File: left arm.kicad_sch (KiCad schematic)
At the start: 11 parts, among them M21 Stepper_Motor_bipolar, M22 Motor_DC, M23 RHP020N06, M24 Motor_Servo, M25 Motor_Servo, M26 Motor_Servo, M27 Stepper_Motor_bipolar, M28 Stepper_Motor_bipolar

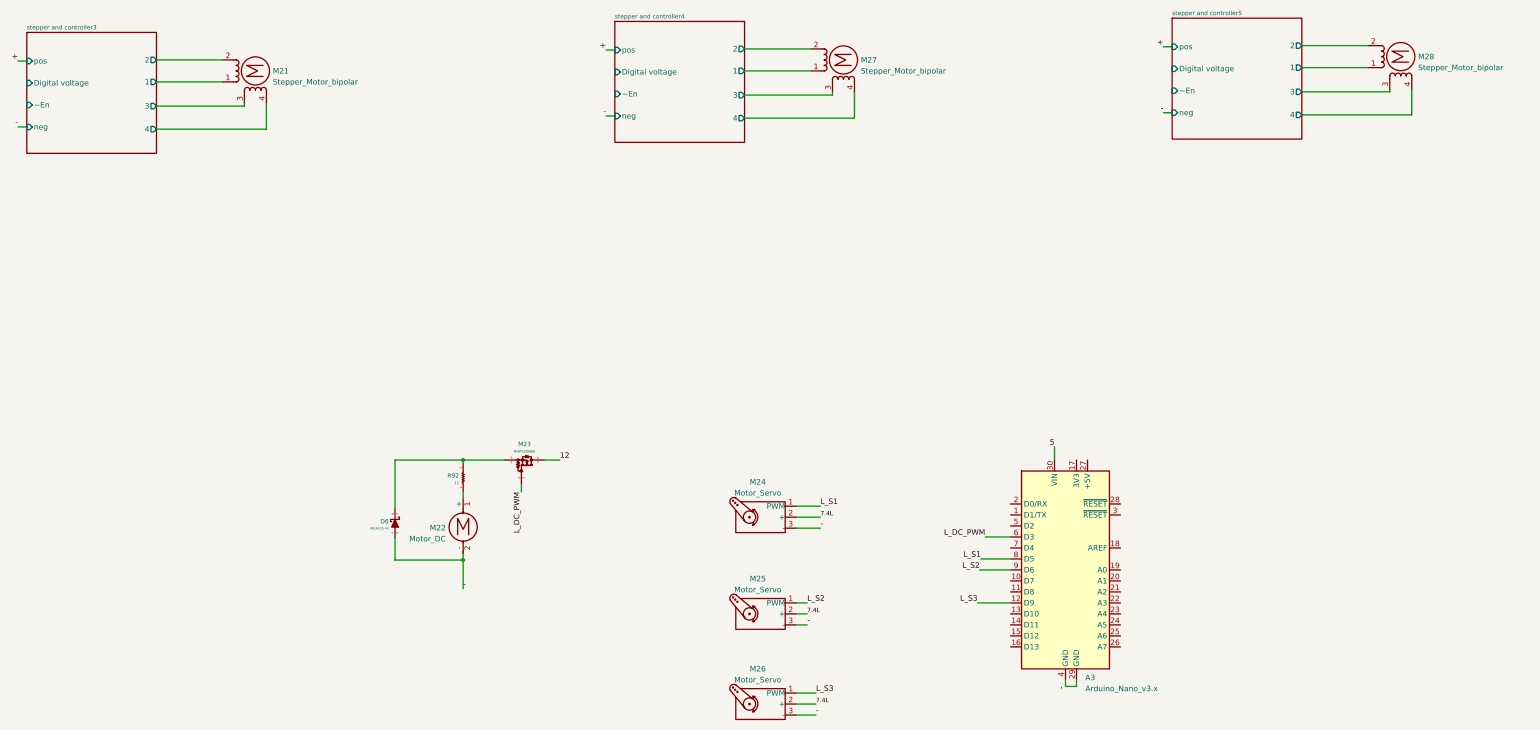
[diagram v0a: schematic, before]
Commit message: base schematic and PCB made
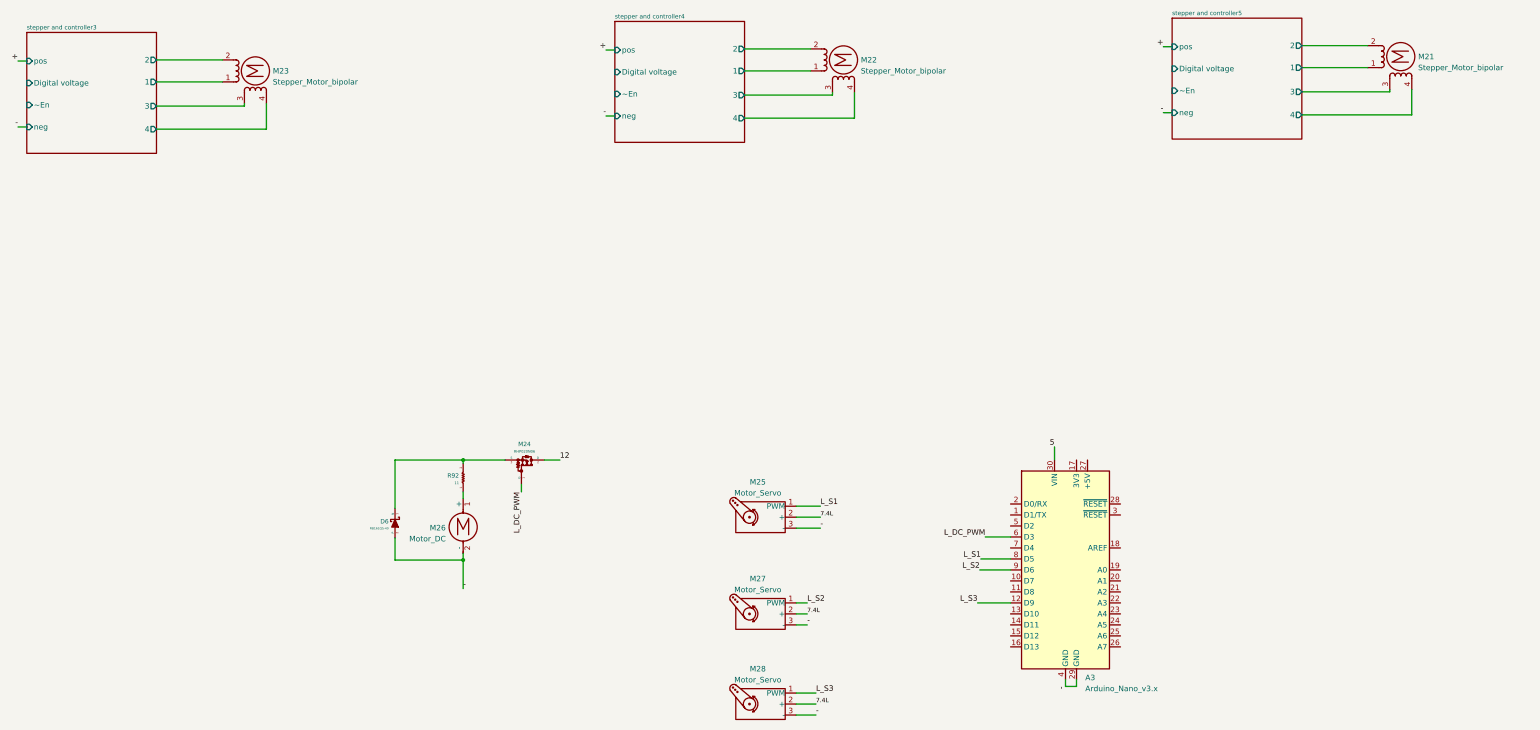
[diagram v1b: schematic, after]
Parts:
- D6: footprint my_footprints:RB161QS-40T18R -> Diodes:RB161QS-40T18R; symbol diodes:RB161QS-40 -> Diodes:RB161QS-40
- M21: renamed from M28; footprint (none) -> Connectors:1-350944-0
- M22: renamed from M27; footprint (none) -> Connectors:1-350944-0
- M23: renamed from M21; footprint (none) -> Connectors:1-350944-0
- M24: renamed from M23; footprint my_footprints:RHP020N06T100 -> E-MOSFETs:RHP020N06T100
- R92: footprint my_footprints:MCR03EZPFX -> Resistors:MCR03EZPFX; symbol resistors:MCR03EZPFX -> Resistors:MCR03EZPFX
- renumbered M24 to M25, M22 to M26, M25 to M27, M26 to M28
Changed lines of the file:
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@@
     (effects (font (size 1 1)) (justify left bottom))
   )
-  (symbol (lib_id "resistors:MCR03EZPFX") (at 131.572 140.208 270) (mirror x) (unit 1)
+  (symbol (lib_id "Resistors:MCR03EZPFX") (at 131.572 140.208 270) (mirror x) (unit 1)
     (in_bom yes) (on_board yes) (fields_autoplaced)
     (property "Reference" "R92" (id 0) (at 130.6068 139.7467 90)
@@
       (effects (font (size 0.6 0.6)) (justify right))
     )
-    (property "Footprint" "my_footprints:MCR03EZPFX" (id 2) (at 123.698 140.208 0)
+    (property "Footprint" "Resistors:MCR03EZPFX" (id 2) (at 123.698 140.208 0)
       (effects (font (size 1.27 1.27)) hide)
     )
@@
     (pin "2")
   )
-  (symbol (lib_id "diodes:RB161QS-40") (at 115.824 150.876 90) (mirror x) (unit 1)
+  (symbol (lib_id "Diodes:RB161QS-40") (at 115.824 150.876 90) (mirror x) (unit 1)
     (in_bom yes) (on_board yes) (fields_autoplaced)
     (property "Reference" "D6" (id 0) (at 114.3508 150.3333 90)
@@
       (effects (font (size 0.5 0.5)) (justify left))
     )
-    (property "Footprint" "my_footprints:RB161QS-40T18R" (id 2) (at 126.492 150.876 0)
+    (property "Footprint" "Diodes:RB161QS-40T18R" (id 2) (at 126.492 150.876 0)
       (effects (font (size 1.524 1.524)) hide)
     )
@@
   (symbol (lib_id "Motor:Motor_Servo") (at 200.914 149.352 0) (mirror y) (unit 1)
     (in_bom yes) (on_board yes) (fields_autoplaced)
-    (property "Reference" "M24" (id 0) (at 199.6551 141.2294 0))
+    (property "Reference" "M25" (id 0) (at 199.6551 141.2294 0))
     (property "Value" "Motor_Servo" (id 1) (at 199.6551 143.7663 0))
     (property "Footprint" "" (id 2) (at 200.914 154.178 0)
@@
   (symbol (lib_id "Motor:Motor_Servo") (at 200.914 192.532 0) (mirror y) (unit 1)
     (in_bom yes) (on_board yes) (fields_autoplaced)
-    (property "Reference" "M26" (id 0) (at 199.6551 184.4094 0))
+    (property "Reference" "M28" (id 0) (at 199.6551 184.4094 0))
     (property "Value" "Motor_Servo" (id 1) (at 199.6551 186.9463 0))
     (property "Footprint" "" (id 2) (at 200.914 197.358 0)
@@
   (symbol (lib_id "Motor:Stepper_Motor_bipolar") (at 348.234 42.926 90) (unit 1)
     (in_bom yes) (on_board yes) (fields_autoplaced)
-    (property "Reference" "M28" (id 0) (at 352.2472 42.9422 90)
+    (property "Reference" "M21" (id 0) (at 352.2472 42.9422 90)
       (effects (font (size 1.27 1.27)) (justify right))
     )
@@
       (effects (font (size 1.27 1.27)) (justify right))
     )
-    (property "Footprint" "" (id 2) (at 348.488 42.672 0)
+    (property "Footprint" "Connectors:1-350944-0" (id 2) (at 348.488 42.672 0)
       (effects (font (size 1.27 1.27)) hide)
     )
@@
   (symbol (lib_id "Motor:Stepper_Motor_bipolar") (at 83.566 46.228 90) (unit 1)
     (in_bom yes) (on_board yes) (fields_autoplaced)
-    (property "Reference" "M21" (id 0) (at 87.5792 46.2442 90)
+    (property "Reference" "M23" (id 0) (at 87.5792 46.2442 90)
       (effects (font (size 1.27 1.27)) (justify right))
     )
@@
       (effects (font (size 1.27 1.27)) (justify right))
     )
-    (property "Footprint" "" (id 2) (at 83.82 45.974 0)
+    (property "Footprint" "Connectors:1-350944-0" (id 2) (at 83.82 45.974 0)
       (effects (font (size 1.27 1.27)) hide)
     )
@@
   (symbol (lib_id "Motor:Motor_DC") (at 131.572 150.114 0) (mirror y) (unit 1)
     (in_bom yes) (on_board yes) (fields_autoplaced)
-    (property "Reference" "M22" (id 0) (at 127.5588 151.8193 0)
+    (property "Reference" "M26" (id 0) (at 127.5588 151.8193 0)
       (effects (font (size 1.27 1.27)) (justify left))
     )
@@
   (symbol (lib_id "Motor:Stepper_Motor_bipolar") (at 219.456 43.688 90) (unit 1)
     (in_bom yes) (on_board yes) (fields_autoplaced)
-    (property "Reference" "M27" (id 0) (at 223.4692 43.7042 90)
+    (property "Reference" "M22" (id 0) (at 223.4692 43.7042 90)
       (effects (font (size 1.27 1.27)) (justify right))
     )
@@
       (effects (font (size 1.27 1.27)) (justify right))
     )
-    (property "Footprint" "" (id 2) (at 219.71 43.434 0)
+    (property "Footprint" "Connectors:1-350944-0" (id 2) (at 219.71 43.434 0)
       (effects (font (size 1.27 1.27)) hide)
     )
@@
   (symbol (lib_id "Motor:Motor_Servo") (at 200.914 171.704 0) (mirror y) (unit 1)
     (in_bom yes) (on_board yes) (fields_autoplaced)
-    (property "Reference" "M25" (id 0) (at 199.6551 163.5814 0))
+    (property "Reference" "M27" (id 0) (at 199.6551 163.5814 0))
     (property "Value" "Motor_Servo" (id 1) (at 199.6551 166.1183 0))
     (property "Footprint" "" (id 2) (at 200.914 176.53 0)
@@
   (symbol (lib_id "E-MOSFETs:RHP020N06") (at 146.304 136.144 270) (mirror x) (unit 1)
     (in_bom yes) (on_board yes) (fields_autoplaced)
-    (property "Reference" "M23" (id 0) (at 145.7456 132.4684 90)
+    (property "Reference" "M24" (id 0) (at 145.7456 132.4684 90)
       (effects (font (size 1 1)))
     )
@@
       (effects (font (size 0.6 0.6)))
     )
-    (property "Footprint" "my_footprints:RHP020N06T100" (id 2) (at 130.81 136.144 0)
+    (property "Footprint" "E-MOSFETs:RHP020N06T100" (id 2) (at 130.81 136.144 0)
       (effects (font (size 1.524 1.524)) hide)
     )
